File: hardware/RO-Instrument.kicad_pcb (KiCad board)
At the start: 2 copper layers, 92.1 x 89.1 mm, 379 parts, among them IC1 MIC5504-2.5YM5-TR, IC10 TCA9517DGKRQ1, IC11 K4F6E3S4HM-MGCJ, IC12 K4F6E3S4HM-MGCJ, IC13 INA226AQDGSRQ1, IC14 TMP112AQDRLRQ1, IC15 W25Q128JVSIQ, IC16 MAX8510EXK29+T, IC17 MAX8510EXK29+T, IC2 TLV62569DBVT, IC3 MIC23303YML-TR, IC4 MIC23303YML-TR, IC5 MIC23303YML-TR, IC6 SN74LVC2G241DCUR, IC7 MAX2771ETI+, IC8 MCP3464RT-E_NC, IC9 TCA9517DGKRQ1, J3 SSQ-126-04-G-D, J4 SSQ-126-04-G-D, Q1 RQ3E120ATTB, Q10 DMG1012T-7, Q11 DMG1012T-7, Q12 DMG1012T-7, Q13 DMG1012T-7, Q14 DMG1012T-7, Q15 DMG1012T-7, Q16 DMG1012T-7, Q17 DMG1012T-7, Q18 DMG1012T-7, Q19 DMG1012T-7, Q2 MMBT3906LT3G, Q20 DMG1012T-7, Q21 DMG1012T-7, Q3 RQ3E120ATTB, Q4 RQ3E120ATTB, Q5 BCM857BS-7-F, Q6 RQ3E120ATTB, Q7 BCM857BS-7-F, Q8 BCM857BS-7-F, Q9 BCM857BS-7-F, U1 ATL431AIDBZR, U10 UM3304, U11 UM3304, U12 UM3304, U13 UM3304, U15 UM3304, U17 UM3304, U2 MIC22950YML-TR, U3 MCP1725T-ADJE/MC, U6 MCP1754ST-3302E/CB, U7 EMMC16G-TB29-PZ90, U8 SN65HVD234QDRQ1

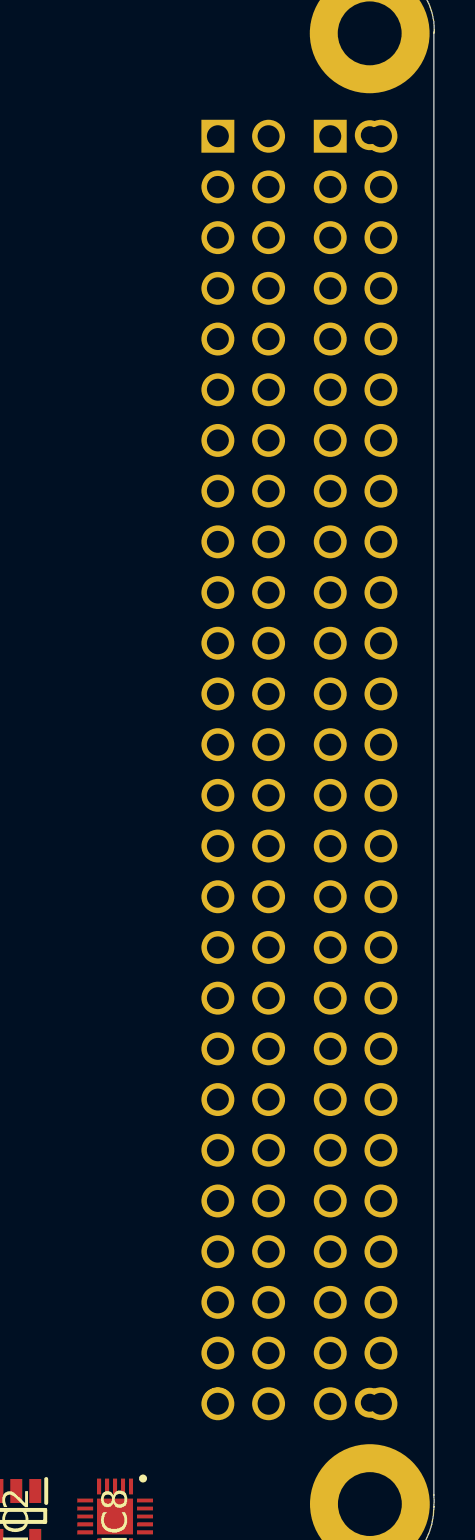
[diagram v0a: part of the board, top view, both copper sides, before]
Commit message: modified PC104 holes and added 3D model
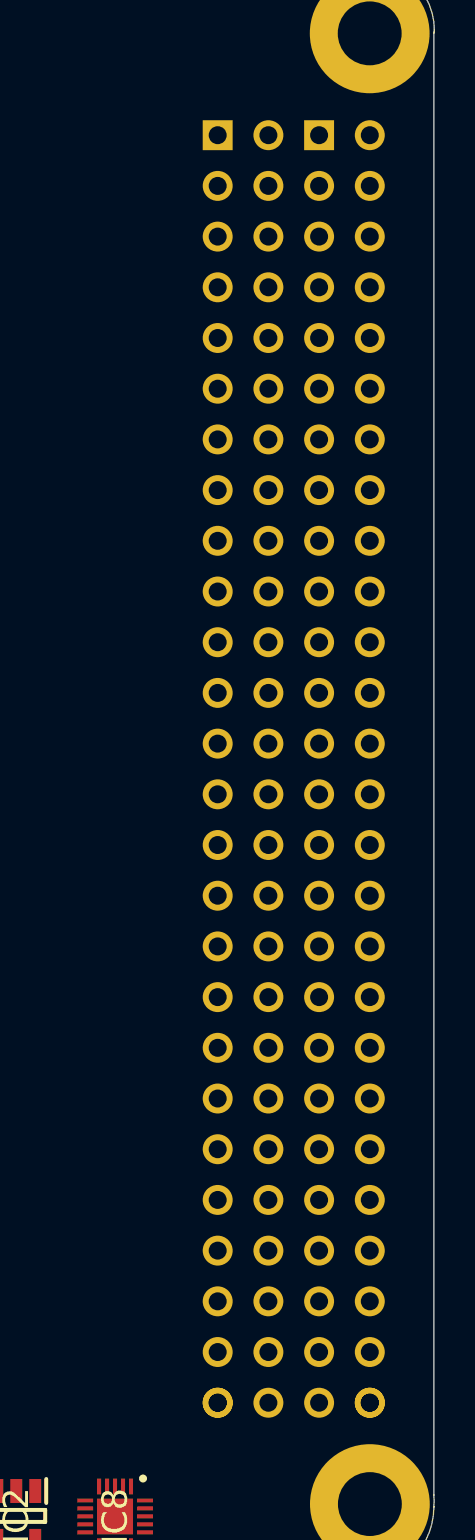
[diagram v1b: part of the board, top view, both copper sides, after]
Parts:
- removed the ? at (249.4, 61.9)
- removed the ? at (257.0, 61.9)
- moved J3 0.56 mm to (254.4, 61.9)
- moved J4 0.05 mm to (249.4, 61.9)

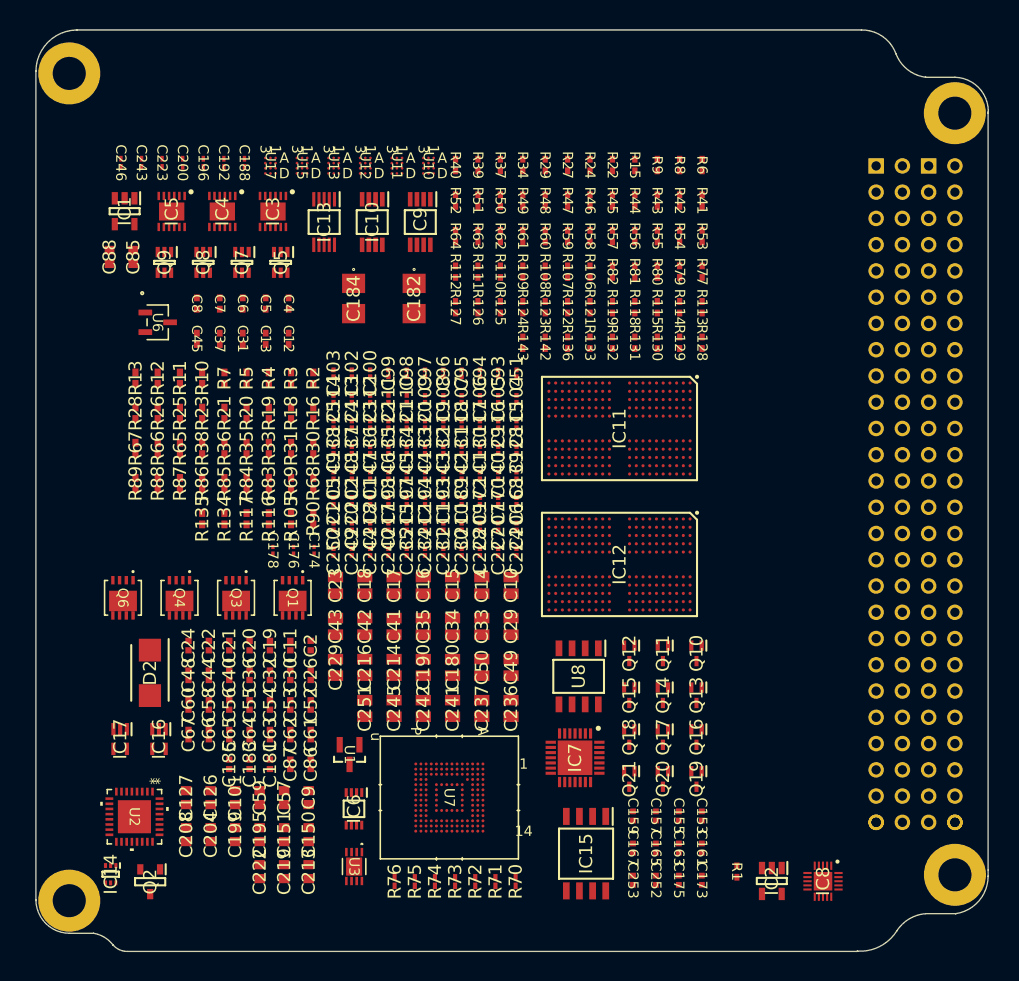
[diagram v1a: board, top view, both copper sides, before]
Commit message: assigned usb resistors and capacitors footprints, created a preliminary 3D PCB model
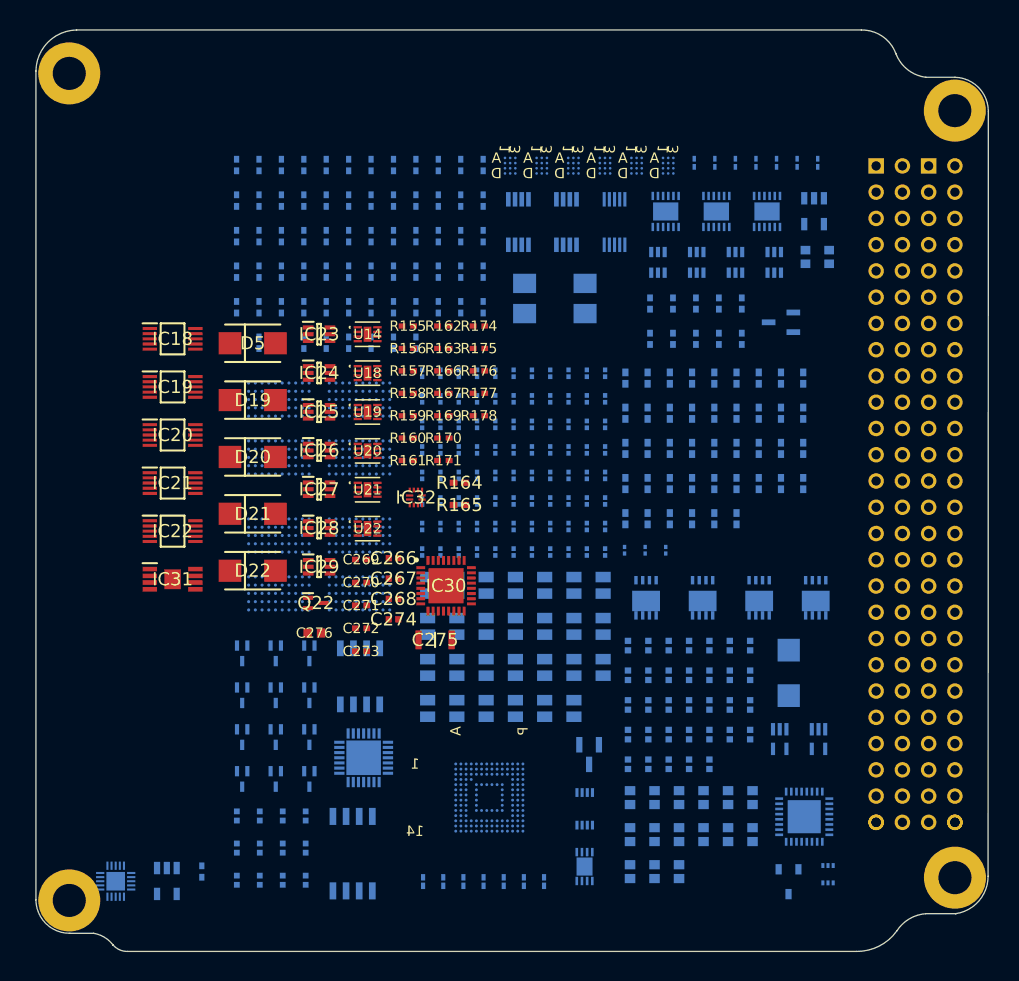
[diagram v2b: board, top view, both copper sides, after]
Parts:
- added C266: 100nF, payload_footprints:CAPC1005X55N, F.Cu at (202.7, 99.9)
- added C267: 100nF, payload_footprints:CAPC1005X55N, F.Cu at (202.7, 101.9)
- added C268: 100nF, payload_footprints:CAPC1005X55N, F.Cu at (202.7, 103.8)
- added C269: 1uF, payload_footprints:YAG_CC0402_YAG, F.Cu at (199.5, 100.0)
- added C270: 1uF, payload_footprints:YAG_CC0402_YAG, F.Cu at (199.5, 102.2)
- added C271: 1uF, payload_footprints:YAG_CC0402_YAG, F.Cu at (199.5, 104.5)
- added C272: 18pF, payload_footprints:YAG_CC0402_YAG, F.Cu at (199.5, 106.7)
- added C273: 18pF, payload_footprints:YAG_CC0402_YAG, F.Cu at (199.5, 108.9)
- added C274: 100nF, payload_footprints:CAPC1005X55N, F.Cu at (202.7, 105.8)
- added C275: 100uF, payload_footprints:CAPC3216X180N, F.Cu at (206.7, 107.8)
- added C276: 2.2uF, payload_footprints:CAP_CC0603_YAG, F.Cu at (195.0, 107.1)
- added D19: SMBJ5.0CA-TR, payload_footprints:SMBJ12A, F.Cu at (189.0, 84.6)
- added D20: SMBJ5.0CA-TR, payload_footprints:SMBJ12A, F.Cu at (189.0, 90.1)
- added D21: SMBJ5.0CA-TR, payload_footprints:SMBJ12A, F.Cu at (189.0, 95.6)
- added D22: SMBJ5.0CA-TR, payload_footprints:SMBJ12A, F.Cu at (189.0, 101.1)
- added D5: SMBJ5.0CA-TR, payload_footprints:SMBJ12A, F.Cu at (189.0, 79.1)
- added IC18: INA226AQDGSRQ1, payload_footprints:SOP50P490X110-10N, F.Cu at (181.3, 78.7)
- added IC19: INA226AQDGSRQ1, payload_footprints:SOP50P490X110-10N, F.Cu at (181.3, 83.3)
- added IC20: INA226AQDGSRQ1, payload_footprints:SOP50P490X110-10N, F.Cu at (181.3, 88.0)
- added IC21: INA226AQDGSRQ1, payload_footprints:SOP50P490X110-10N, F.Cu at (181.3, 92.6)
- added IC22: INA226AQDGSRQ1, payload_footprints:SOP50P490X110-10N, F.Cu at (181.3, 97.3)
- added IC23: SI1416EDH-T1-GE3, payload_footprints:SOT65P210X110-6N, F.Cu at (195.5, 78.2)
- added IC24: SI1416EDH-T1-GE3, payload_footprints:SOT65P210X110-6N, F.Cu at (195.5, 82.0)
- added IC25: SI1416EDH-T1-GE3, payload_footprints:SOT65P210X110-6N, F.Cu at (195.5, 85.7)
- added IC26: SI1416EDH-T1-GE3, payload_footprints:SOT65P210X110-6N, F.Cu at (195.5, 89.5)
- added IC27: SI1416EDH-T1-GE3, payload_footprints:SOT65P210X110-6N, F.Cu at (195.5, 93.2)
- added IC28: SI1416EDH-T1-GE3, payload_footprints:SOT65P210X110-6N, F.Cu at (195.5, 97.0)
- added IC29: SI1416EDH-T1-GE3, payload_footprints:SOT65P210X110-6N, F.Cu at (195.5, 100.7)
- added IC30: USB3340-EZK-TR, payload_footprints:QFN50P500X500X100-33N-D, F.Cu at (207.7, 102.6)
- added IC31: TPS2051BDGN, payload_footprints:SOP65P490X110-9N, F.Cu at (181.3, 101.9)
- added IC32: PTN5150AHXMP, payload_footprints:PTN5150AHXMP, F.Cu at (204.8, 94.0)
- added Q22: DMG1012T-7, payload_footprints:SOT50P160X90-3N, F.Cu at (195.1, 104.2)
- added R155: 10K, payload_footprints:RC0402N_YAG, F.Cu at (204.0, 77.4)
- added R156: 10K, payload_footprints:RC0402N_YAG, F.Cu at (204.0, 79.6)
- added R157: 10K, payload_footprints:RC0402N_YAG, F.Cu at (204.0, 81.8)
- added R158: 10K, payload_footprints:RC0402N_YAG, F.Cu at (204.0, 83.9)
- added R159: 10K, payload_footprints:RC0402N_YAG, F.Cu at (204.0, 86.1)
- added R160: 10K, payload_footprints:RC0402N_YAG, F.Cu at (204.0, 88.3)
- added R161: 10K, payload_footprints:RC0402N_YAG, F.Cu at (204.0, 90.4)
- added R162: 10K, payload_footprints:RC0402N_YAG, F.Cu at (207.5, 77.4)
- added R163: 0R, payload_footprints:RC0402N_YAG, F.Cu at (207.5, 79.6)
- added R164: 27R, payload_footprints:RESC1005X40N, F.Cu at (209.0, 92.6)
- added R165: 8.06K, payload_footprints:RESC1005X40N, F.Cu at (209.0, 94.7)
- added R166: 0R, payload_footprints:RC0402N_YAG, F.Cu at (207.5, 81.8)
- added R167: 1M, payload_footprints:RC0402N_YAG, F.Cu at (207.5, 83.9)
- added R169: 0R, payload_footprints:RC0402N_YAG, F.Cu at (207.5, 86.1)
- added R170: 0R, payload_footprints:RC0402N_YAG, F.Cu at (207.5, 88.3)
- added R171: 0R, payload_footprints:RC0402N_YAG, F.Cu at (207.5, 90.4)
- added R174: 10K, payload_footprints:RC0402N_YAG, F.Cu at (210.9, 77.4)
- added R175: 10K, payload_footprints:RC0402N_YAG, F.Cu at (210.9, 79.6)
- added R176: 10K, payload_footprints:RC0402N_YAG, F.Cu at (210.9, 81.8)
- added R177: 33R, payload_footprints:RC0402N_YAG, F.Cu at (210.9, 83.9)
- added R178: 1K, payload_footprints:RC0402N_YAG, F.Cu at (210.9, 86.1)
- added U14: LTC4361HDC-2-TRMPBF, payload_footprints:DFN-8_DC_LIT, F.Cu at (200.2, 78.2)
- added U18: LTC4361HDC-2-TRMPBF, payload_footprints:DFN-8_DC_LIT, F.Cu at (200.2, 82.0)
- added U19: LTC4361HDC-2-TRMPBF, payload_footprints:DFN-8_DC_LIT, F.Cu at (200.2, 85.8)
- added U20: LTC4361HDC-2-TRMPBF, payload_footprints:DFN-8_DC_LIT, F.Cu at (200.2, 89.5)
- added U21: LTC4361HDC-2-TRMPBF, payload_footprints:DFN-8_DC_LIT, F.Cu at (200.2, 93.3)
- added U22: LTC4361HDC-2-TRMPBF, payload_footprints:DFN-8_DC_LIT, F.Cu at (200.2, 97.0)
- C10, C100, C101, C102, C103, C104, C105, C106, C107, C108, C109, C11, C110, C111, C112, C113, C114, C115, C116, C117, C118, C119, C12, C120, C121, C122, C123, C124, C125, C126, C127, C128, C129, C13, C130, C131, C132, C133, C134, C135, C136, C137, C138, C139, C14, C140, C141, C142, C143, C144, C145, C146, C147, C148, C149, C15, C150, C151, C153, C155, C157, C159, C16, C161, C163, C165, C167, C168, C17, C170, C172, C173, C174, C175, C176, C178, C18, C180, C181, C182, C183, C184, C185, C188, C189, C19, C190, C192, C193, C194, C195, C196, C197, C198, C199, C2, C20, C200, C201, C202, C204, C205, C206, C207, C208, C209, C21, C210, C211, C212, C213, C214, C215, C216, C217, C218, C219, C22, C220, C221, C222, C223, C224, C227, C228, C229, C23, C230, C231, C234, C235, C236, C237, C24, C240, C241, C242, C243, C244, C245, C246, C249, C250, C251, C252, C253, C26, C29, C30, C31, C32, C33, C34, C35, C36, C37, C4, C40, C41, C42, C43, C44, C45, C48, C49, C5, C50, C51, C52, C53, C54, C55, C56, C57, C58, C59, C6, C60, C61, C62, C63, C64, C65, C66, C67, C7, C8, C85, C86, C87, C88, C9, C93, C94, C95, C96, C97, C98, C99, D2, IC1, IC10, IC11, IC12, IC13, IC14, IC15, IC16, IC17, IC2, IC3, IC4, IC5, IC6, IC7, IC8, IC9, Q1, Q10, Q11, Q12, Q13, Q14, Q15, Q16, Q17, Q18, Q19, Q2, Q20, Q21, Q3, Q4, Q5, Q6, Q7, Q8, Q9, R1, R10, R105, R106, R107, R108, R109, R11, R110, R111, R112, R113, R114, R115, R116, R117, R118, R119, R12, R121, R122, R123, R124, R125, R126, R127, R128, R129, R13, R130, R131, R132, R133, R134, R135, R136, R142, R143, R15, R16, R18, R19, R2, R20, R21, R22, R23, R24, R25, R26, R27, R28, R29, R3, R30, R31, R33, R34, R35, R36, R37, R38, R39, R4, R40, R41, R42, R43, R44, R45, R46, R47, R48, R49, R5, R50, R51, R52, R53, R54, R55, R56, R57, R58, R59, R6, R60, R61, R62, R63, R64, R65, R66, R67, R68, R69, R7, R70, R71, R72, R73, R74, R75, R76, R77, R79, R8, R80, R81, R82, R83, R84, R85, R86, R87, R88, R89, R9, R90, U1, U10, U11, U12, U13, U15, U17, U2, U3, U6, U7, U8: moved to B.Cu
- moved C88 69.6 mm to (244.8, 70.8)
- moved IC14 69.4 mm to (244.7, 130.5)
- moved IC8 68.4 mm to (175.8, 131.1)
- moved IC17 67.6 mm to (243.8, 117.4)
- moved C246 67.4 mm to (243.7, 61.6)
- moved Q6 67.0 mm to (243.5, 103.7)
- moved IC1 66.7 mm to (243.3, 66.3)
- moved C85 65.0 mm to (242.5, 70.8)
- moved U2 64.8 mm to (242.4, 124.9)
- moved R13 64.6 mm to (242.3, 82.5)
- moved R28 64.6 mm to (242.3, 85.9)
- moved R67 64.6 mm to (242.3, 89.3)
- moved R89 64.6 mm to (242.3, 92.7)
- moved C243 63.4 mm to (241.7, 61.6)
- moved D2 61.8 mm to (240.9, 111.0)
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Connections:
- net /ME_PERST0n renamed /I2C1_SCL
- net /USB0_RESETB renamed /I2C1_SDA
- IC6 pad 5: unconnected-(IC6-2A-Pad5) -> /UART0_TXD
- IC6 pad 6: unconnected-(IC6-1Y-Pad6) -> /UART0_RXD
- J3 pad 20: /POWER_ENABLE -> unconnected-(J3-H1_20-Pad20)
- J3 pad 41: unconnected-(J3-H1_41-Pad41) -> /PL_I2C_SDA
- J3 pad 43: unconnected-(J3-H1_43-Pad43) -> /PL_I2C_SLC
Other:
- outline, holes or cut-outs redrawn

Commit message: fixed step files
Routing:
- added copper zone on F.Cu, net GNDREF
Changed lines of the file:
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@@
 		(layer "Edge.Cuts")
+	)
+	(zone
+		(net "GNDREF")
+		(layer "F.Cu")
+		(hatch edge 0.5)
+		(connect_pads yes
+			(clearance 0.5)
+		)
+		(min_thickness 0.25)
+		(fill yes
+			(thermal_gap 0.5)
+			(thermal_bridge_width 0.5)
+			(island_removal_mode 0)
+		)
+		(polygon
+			(pts
+				(xy 167.2 47.9) (xy 261.2 48) (xy 261.2 138.8) (xy 166.6 138.8)
+			)
+		)
 	)
 	(embedded_fonts no)

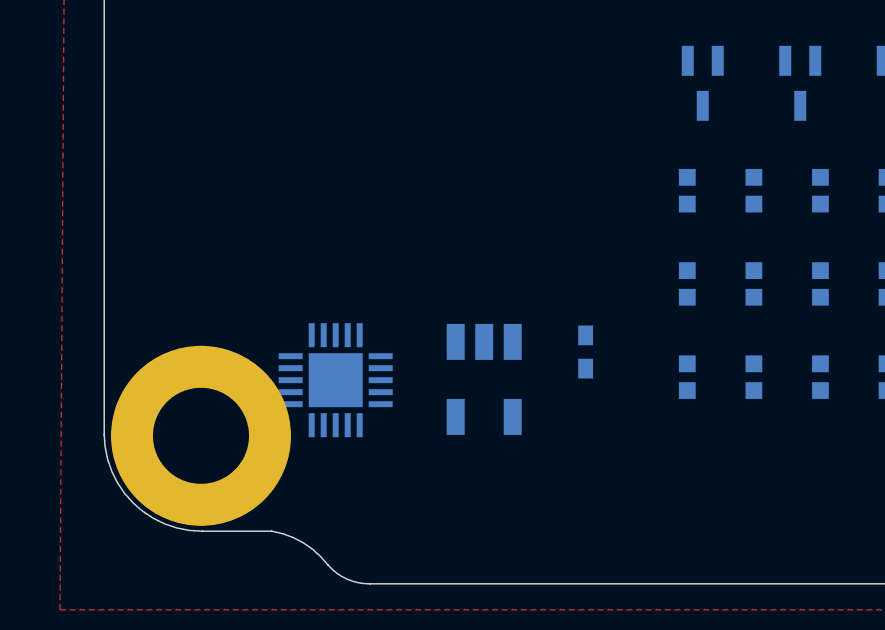
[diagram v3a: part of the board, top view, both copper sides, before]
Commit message: modified preliminary PCB 3D model for satellite CAD
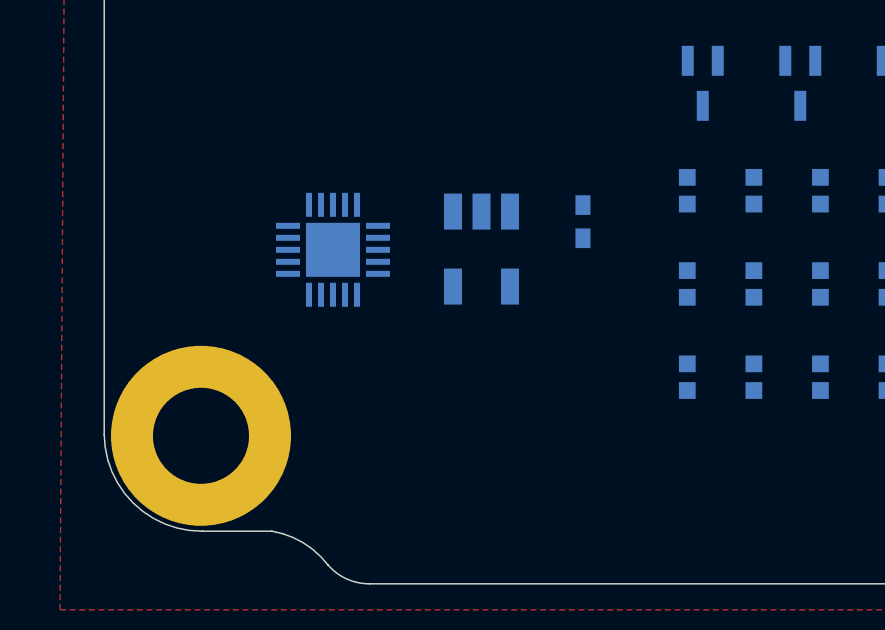
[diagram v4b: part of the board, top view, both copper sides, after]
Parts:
- moved IC8 4.35 mm to (175.7, 126.8)
- moved R1 4.35 mm to (184.0, 125.9)
- moved IC2 4.35 mm to (180.7, 126.8)
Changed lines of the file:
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@@
 	(footprint "payload_footprints:RC0402N_PAN"
 		(layer "B.Cu")
-		(at 184.120612 130.205799 -90)
+		(at 184.0302 125.860799 -90)
 		(tags "ERJ-2RKF5102X ")
 		(property "Reference" "R1"
@@
 			(polygon
 				(pts
-					(xy 183.921412 130.031599) (xy 183.921412 130.379999) (xy 184.319812 130.379999) (xy 184.319812 130.031599)
+					(xy 183.831 125.686599) (xy 183.831 126.034999) (xy 184.2294 126.034999) (xy 184.2294 125.686599)
 				)
 			)
@@
 	(footprint "payload_footprints:SOT95P280X145-5N"
 		(layer "B.Cu")
-		(at 180.740412 131.12 -90)
+		(at 180.65 126.775 -90)
 		(descr "DBV")
 		(tags "Integrated Circuit")
@@
 	(footprint "payload_footprints:QFN40P300X300X60-21N-D"
 		(layer "B.Cu")
-		(at 175.790412 131.145 -90)
+		(at 175.7 126.8 -90)
 		(descr "20 Lead QFN (NC)-3x3")
 		(tags "Integrated Circuit")
